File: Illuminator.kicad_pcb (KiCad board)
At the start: 2 copper layers, 58.5 x 58.5 mm, 30 parts, among them J0 Conn_02x03_Top_Bottom, Q0 DMG1012UW, U1 VEML7700

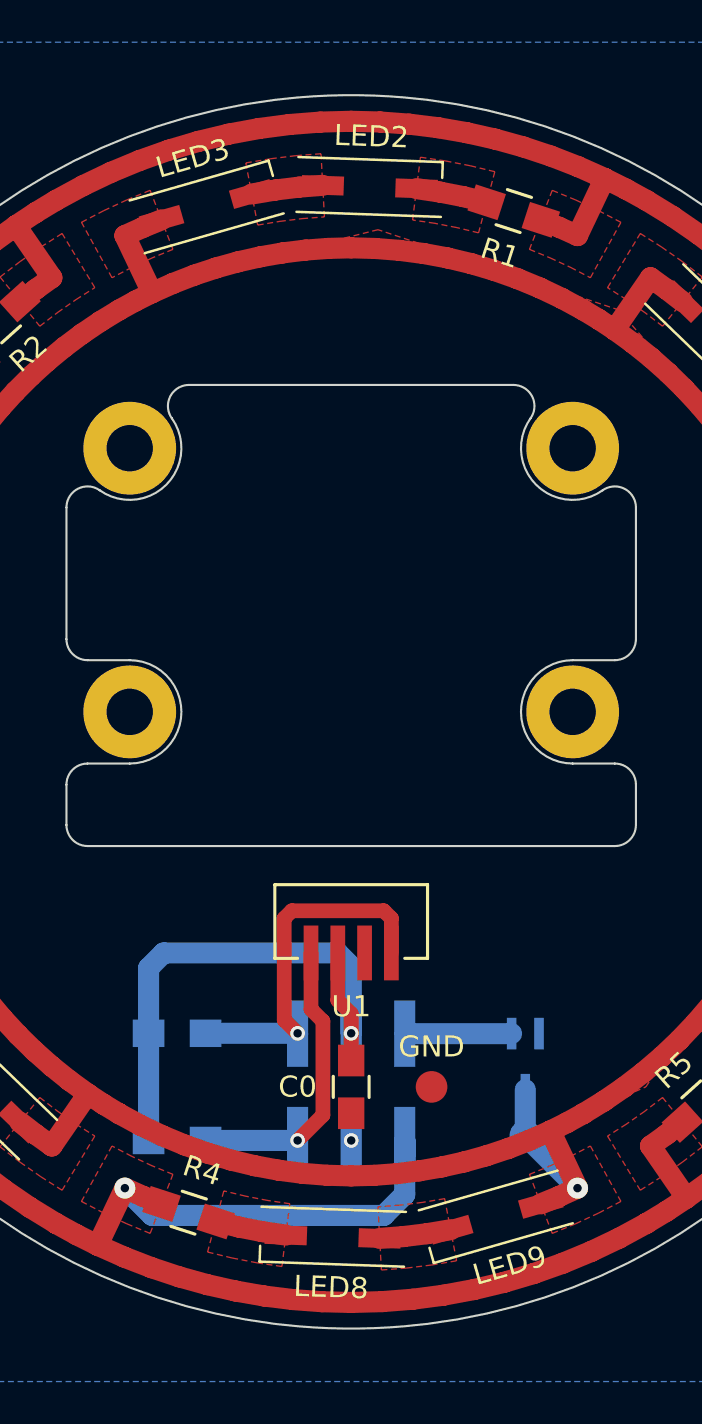
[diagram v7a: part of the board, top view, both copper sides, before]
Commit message: Added QR code, Mittelab logo and OpenHardware logo
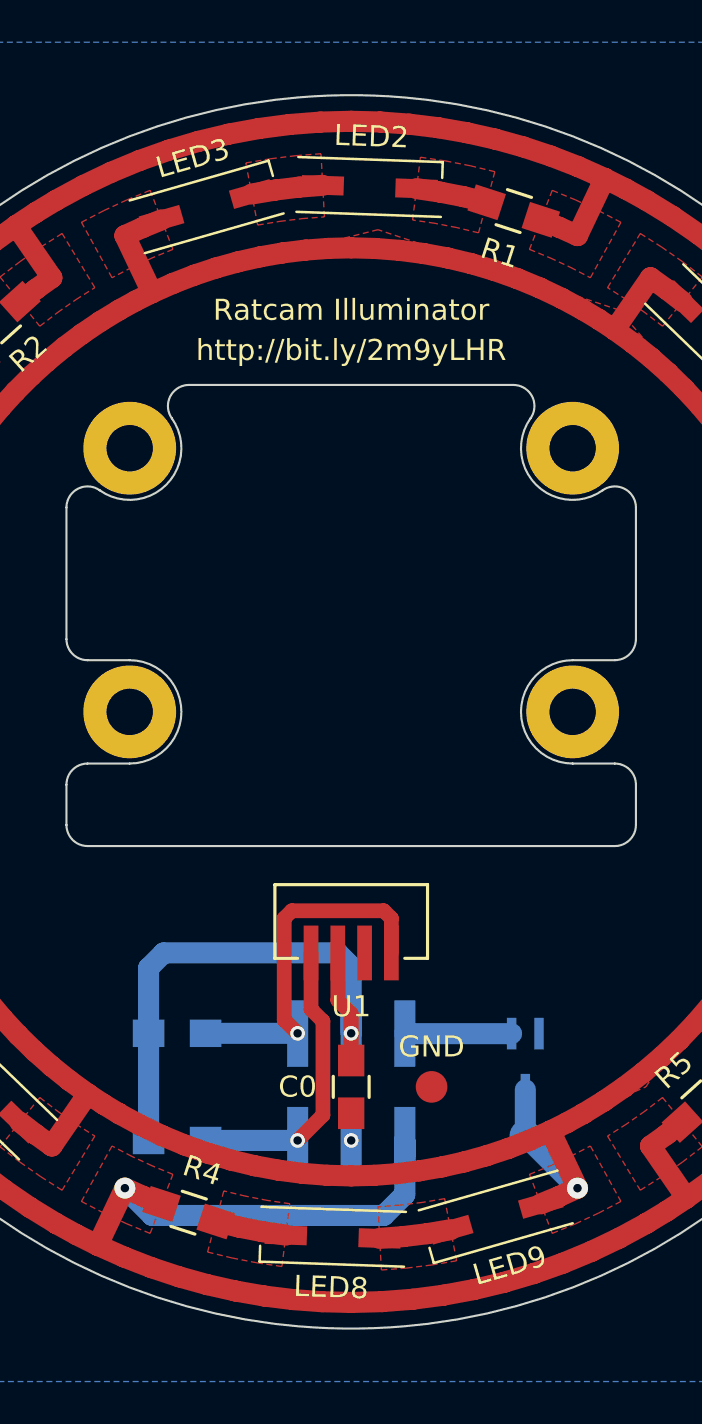
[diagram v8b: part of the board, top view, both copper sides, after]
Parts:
- added Mittelab: Mittelab, Ratcam:MittelabLogo, B.Cu at (121.1, 100.1)
- added OSHW: OpenSourceHardware, Ratcam:OSHWLogo, B.Cu at (78.9, 100.0)
- added QRCode: Ratcam Illuminator, Ratcam:QRCode, B.Cu at (100.0, 77.8)
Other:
- board text added: "http://bit.ly/2m9yLHR"
